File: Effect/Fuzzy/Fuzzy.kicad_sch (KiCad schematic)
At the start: 16 parts, among them J1 Conn_01x04_Pin, Q1 MMBFJ201

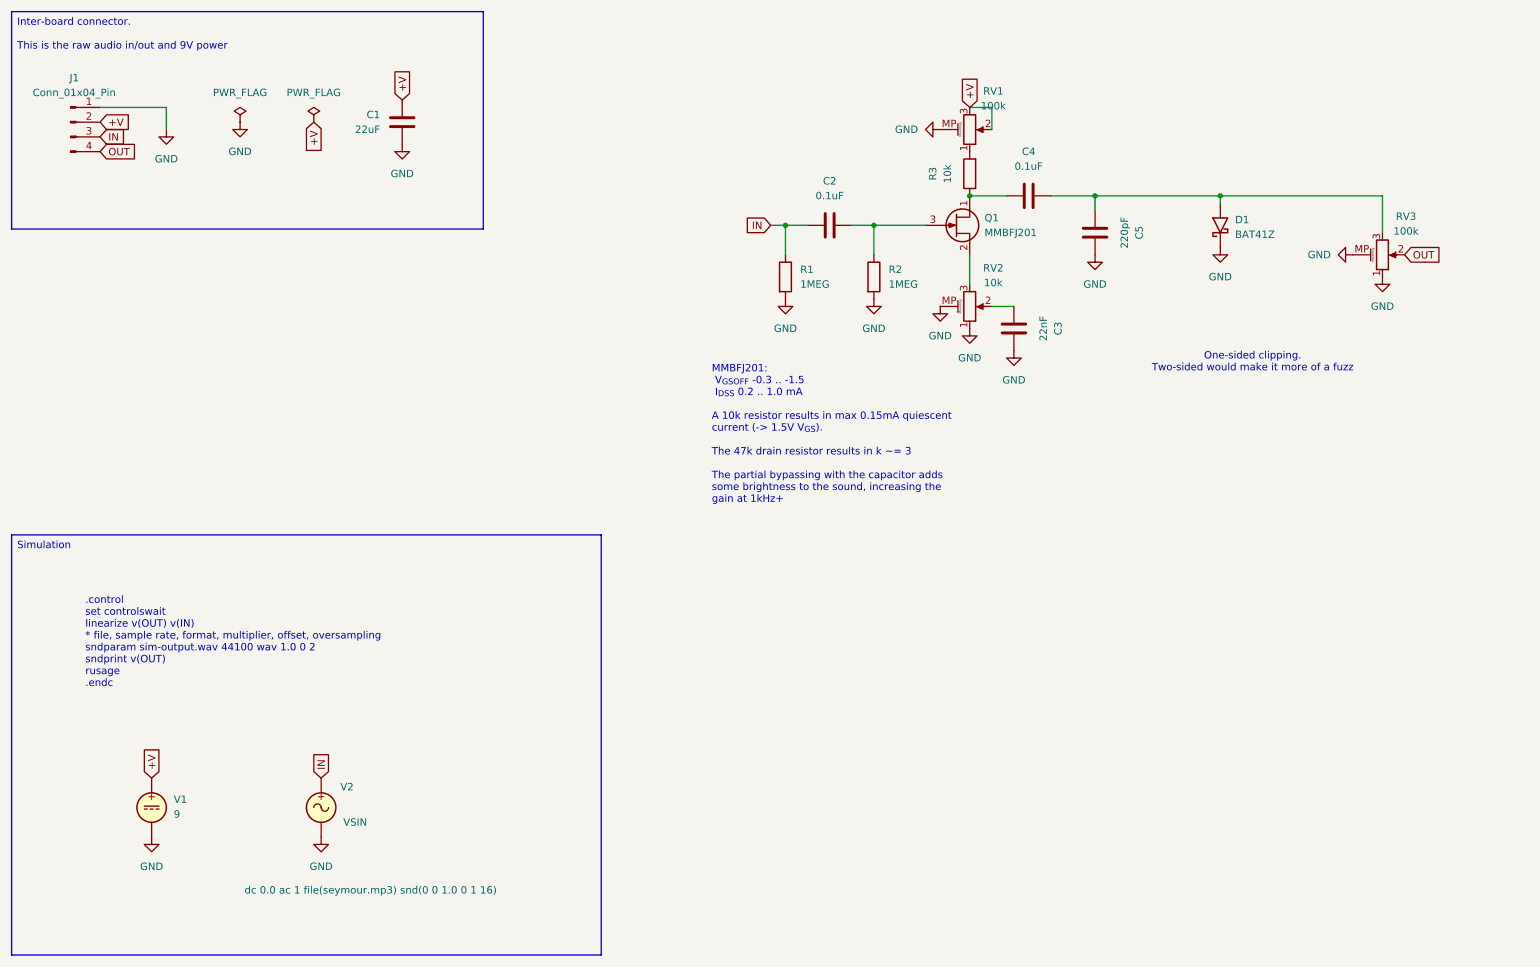
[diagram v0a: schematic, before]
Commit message: First revisions from gen3 testing...
It turns out that while the single connector was sufficient, it is also
mechanically annoyingly less robust than the two separate pin headers we
used to have.

So even though we don't need the extra pins, just split it up into
"power" and a "signal" connectors again.  The placement behind the
output jack was good, so just put the power jack behind the input one
instead.

That ends up making routing nicer with the power trace going down where
it needs to be for the LED anyway, so it's a win-win.  Much nicer than
the old board.  And with the extra pins and the position right next to
the LED, lets just make the base board LED voltage available as an
"active" signal in case anybody ever wants it.

Also, just move the DC blocking capacitor and the anti-pop resistor to
ground to the base board.  Any effects board needs to do that, so it's
one less thing to worry about.  Also add back the low pass RF filter.

With the connector change, this obviously makes the new boards
incompatible, but it's not like I have any legacy boards except for the
test-boards.

On the effect board side, this does the layout changes, but also fixes
the Octaver board that was half-arsed and hadn't done proper bias
voltage calculations.  This basically just reuses them from the boost
board.

Plus use a JFET input on for the Octaver, and while at it make it also
just split the phase the natural way.  Both simpler and more balanced.

So maybe the Octaver works now.

And by "works", I obviously don't mean "sounds good".

Signed-off-by: Linus Torvalds <torvalds@linux-foundation.org>
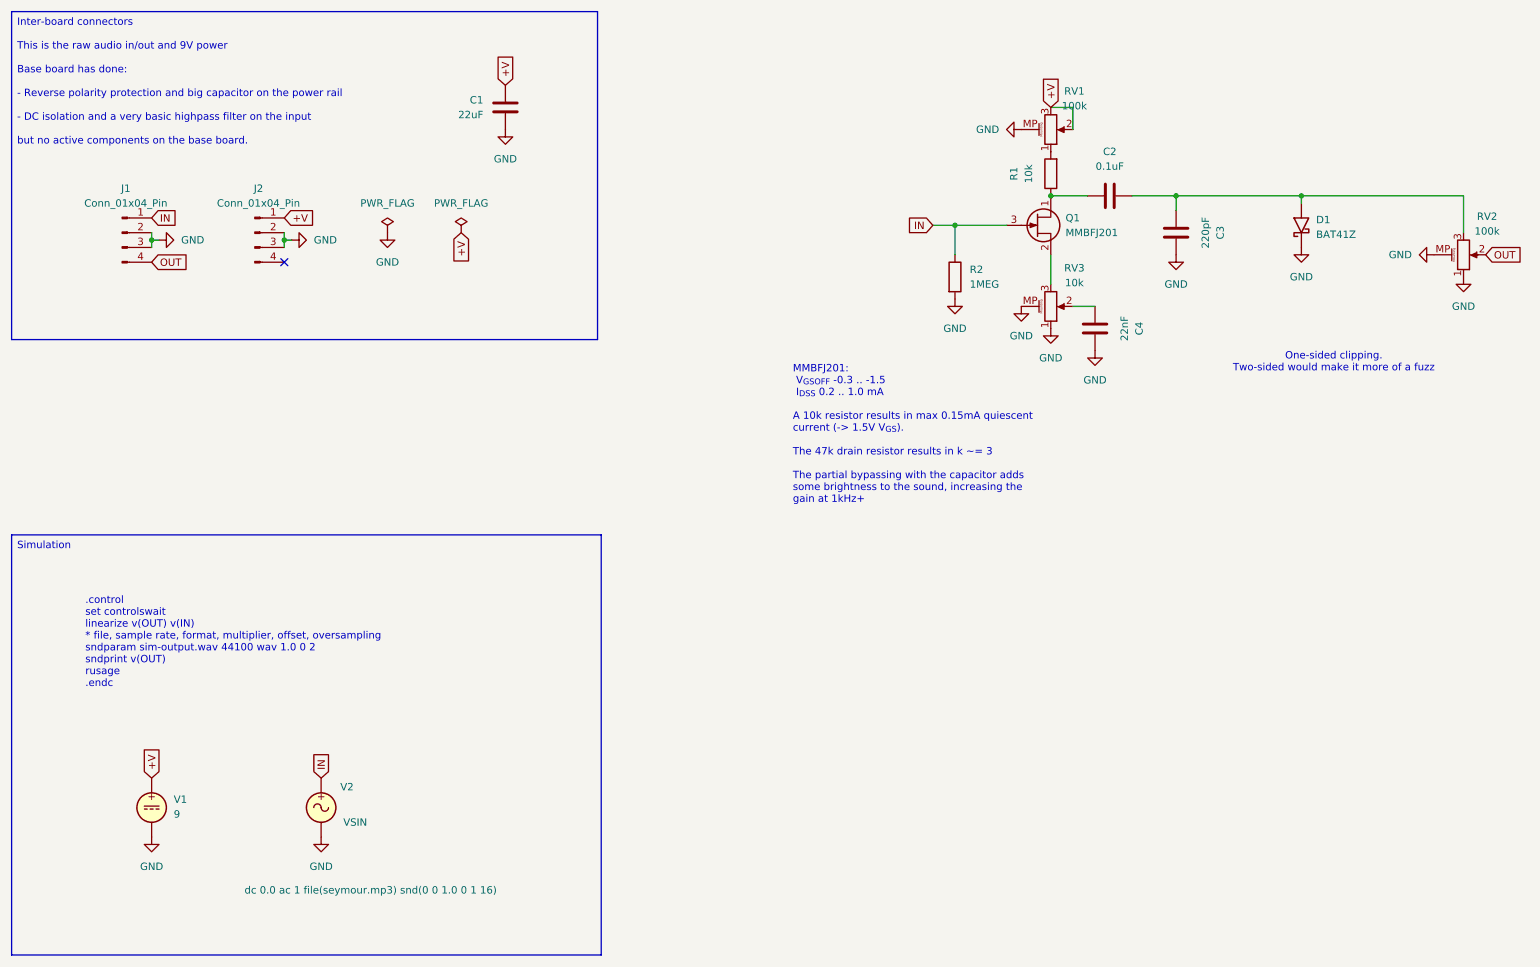
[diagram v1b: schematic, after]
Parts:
- removed C2: 0.1uF, Mylib:C_0704_1810Metric, symbol Device:C
- removed R1: 1MEG, Resistor_SMD:R_0805_2012Metric_Pad1.20x1.40mm_HandSolder, symbol Device:R
- added J2: Conn_01x04_Pin, Connector_PinHeader_2.54mm:PinHeader_1x04_P2.54mm_Vertical, symbol Connector:Conn_01x04_Pin
- renumbered C4 to C2, C5 to C3, C3 to C4, R3 to R1, RV3 to RV2, RV2 to RV3
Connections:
- net +V: now also J2.1 (Pin_1); no longer J1.2 (Pin_2)
- net GND: now also J1.2 (Pin_2), J1.3 (Pin_3), J2.2 (Pin_2), J2.3 (Pin_3); no longer J1.1 (Pin_1)
- net IN: now also J1.1 (Pin_1), Q1.3 (G), R2.1; no longer J1.3 (Pin_3)
- no-connect marks 0 -> 1
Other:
- moved on the sheet: C2, C3, C4, D1, Q1, R1, R2, RV1, RV2, RV3
